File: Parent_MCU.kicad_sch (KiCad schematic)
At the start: 56 parts, among them Y1 Crystal_GND24

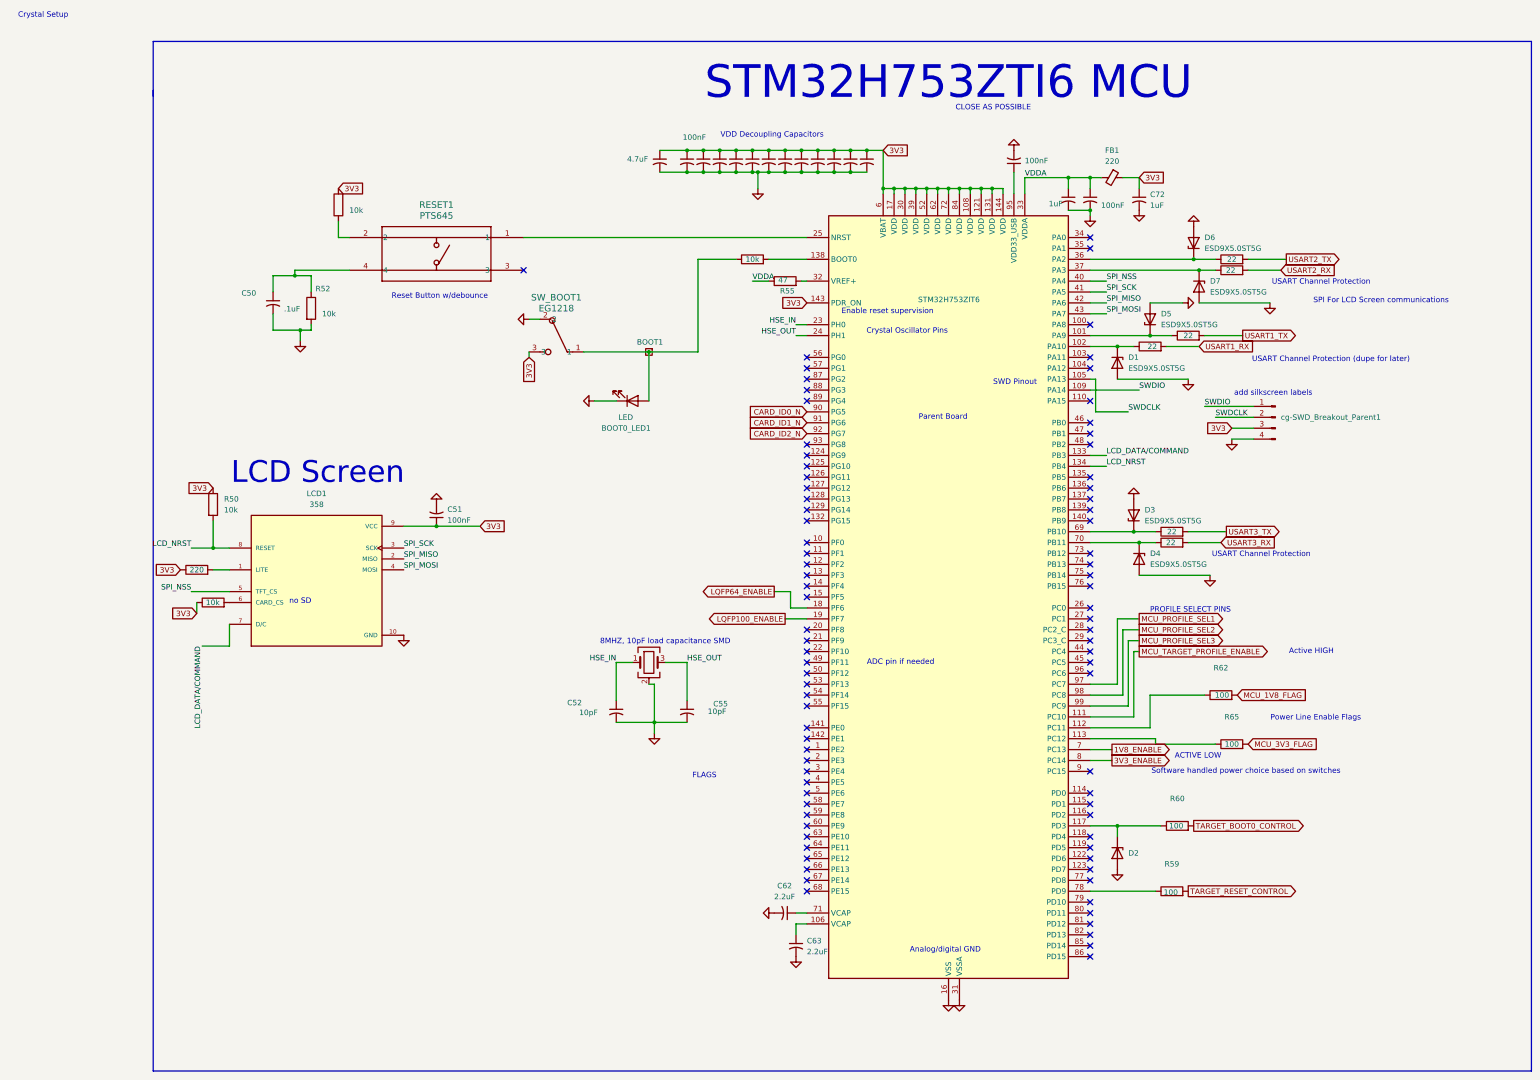
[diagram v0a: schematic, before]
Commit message: finished routing
//TODO
-> add mechanical support
-> daughter board
-> recheck nodes/conections
-> silk screen
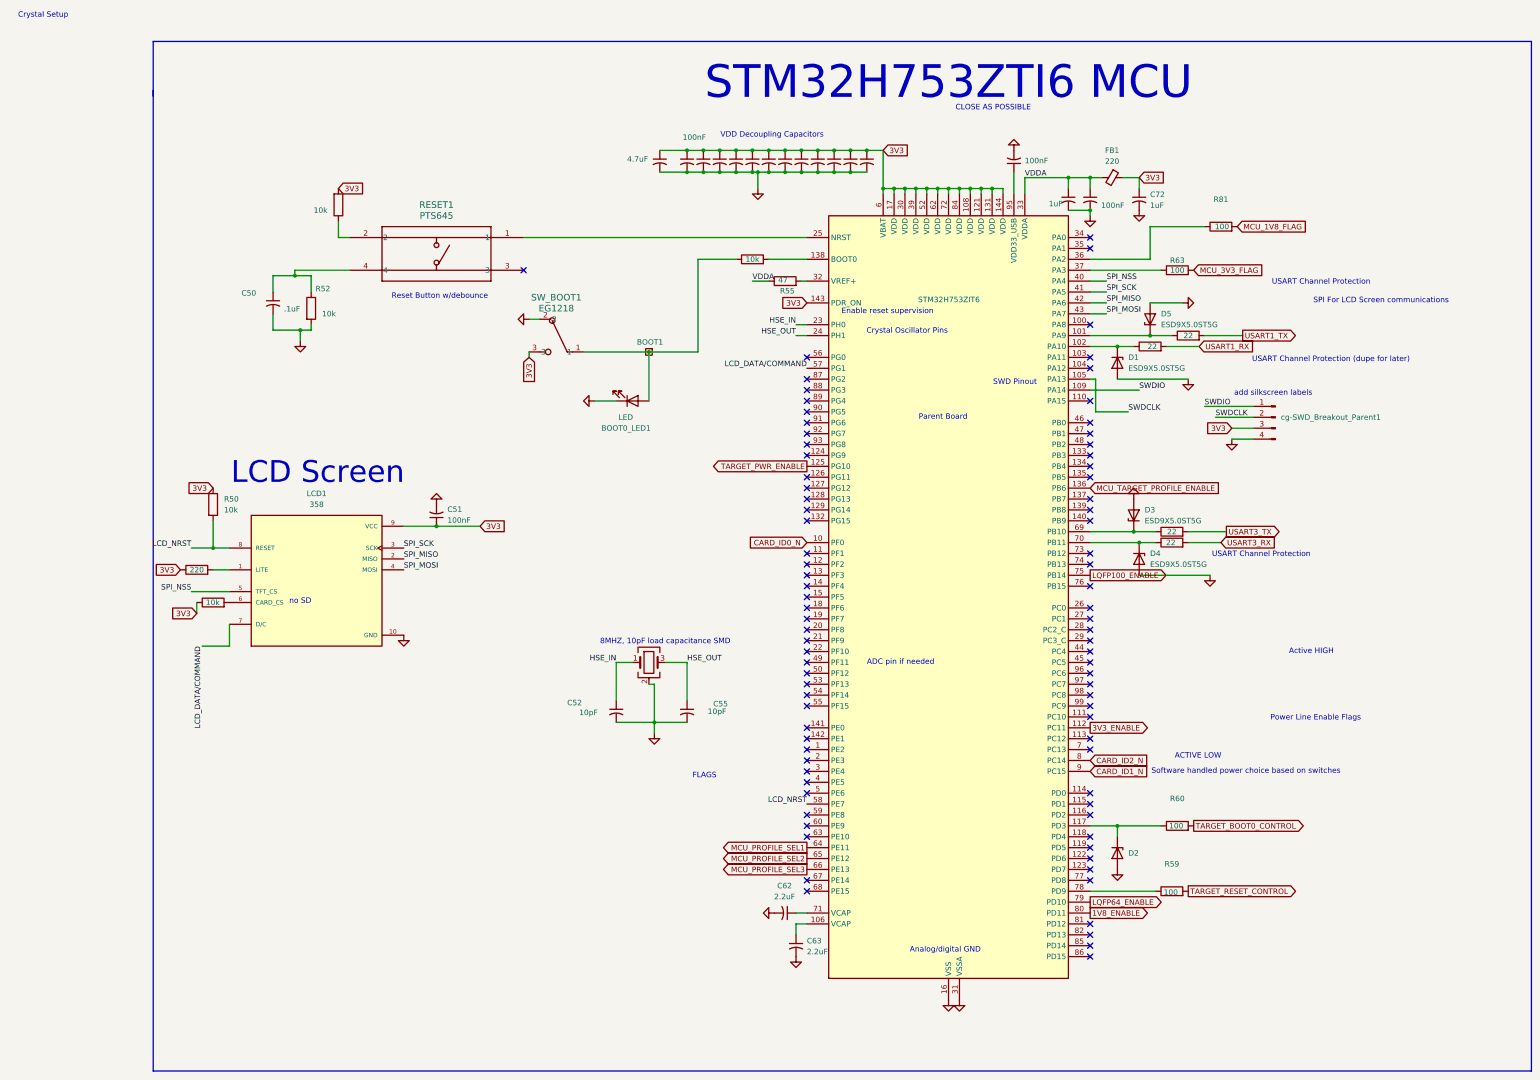
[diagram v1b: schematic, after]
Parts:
- removed D6, D7: ESD9X5.0ST5G, Diode_SMD:D_SOD-923, symbol Diode:PTVS5V0Z1USK
- removed R62, R65: 100, Resistor_SMD:R_0603_1608Metric, symbol Device:R
- removed R64: 22, Resistor_SMD:R_0603_1608Metric, symbol Device:R
- added R81: 100, Resistor_SMD:R_0603_1608Metric, symbol Device:R
- R63: value 22 -> 100
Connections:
- net USART2_TX is gone; now on net MCU_3V3_FLAG: R63.2
- net 1V8_ENABLE: now also STM32H1.80 (PD11); no longer STM32H1.7 (PC13)
- net 3V3_ENABLE: now also STM32H1.112 (PC11); no longer STM32H1.8 (PC14)
- net CARD_ID0_N: now also STM32H1.10 (PF0); no longer STM32H1.90 (PG5)
- net CARD_ID1_N: now also STM32H1.9 (PC15); no longer STM32H1.91 (PG6)
- net CARD_ID2_N: now also STM32H1.8 (PC14); no longer STM32H1.92 (PG7)
- net LCD_DATA/COMMAND: now also STM32H1.57 (PG1); no longer STM32H1.133 (PB3)
- net LCD_NRST: now also STM32H1.58 (PE7); no longer STM32H1.134 (PB4)
- net LQFP100_ENABLE: now also STM32H1.75 (PB14); no longer STM32H1.19 (PF7)
- net LQFP64_ENABLE: now also STM32H1.79 (PD10); no longer STM32H1.18 (PF6)
- net MCU_1V8_FLAG: now also R81.2
- net MCU_PROFILE_SEL1: now also STM32H1.64 (PE11); no longer STM32H1.97 (PC7)
- net MCU_PROFILE_SEL2: now also STM32H1.65 (PE12); no longer STM32H1.98 (PC8)
- net MCU_PROFILE_SEL3: now also STM32H1.66 (PE13); no longer STM32H1.99 (PC9)
- net MCU_TARGET_PROFILE_ENABLE: now also STM32H1.136 (PB6); no longer STM32H1.111 (PC10)
- net at STM32H1.36 (PA2): now also R81.1; no longer R63.1
- net TARGET_PWR_ENABLE: now reaches STM32H1.125 (PG10)
- net at STM32H1.37 (PA3): now also R63.1
- no-connect marks 84 -> 85
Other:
- note removed: "PROFILE SELECT PINS"

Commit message: sockets
fdsfd
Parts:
- renumbered R63 to R60, R60 to R61, R61 to R62, R81 to R63
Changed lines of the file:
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@@
 		(in_pos_files yes)
 		(dnp no)
-		(property "Reference" "R60"
+		(property "Reference" "R61"
 			(at 273.05 200.66 90)
 			(show_name no)
@@
 			(project "CG Files"
 				(path "/bab4cc86-0c89-4bf5-848e-e99340a6180d/d2a8d785-8eb6-410a-b71c-0410f8135e6c"
-					(reference "R60")
+					(reference "R61")
 					(unit 1)
 				)
@@
 		(in_pos_files yes)
 		(dnp no)
-		(property "Reference" "R63"
+		(property "Reference" "R60"
 			(at 273.05 75.184 90)
 			(show_name no)
@@
 			(project "CG Files"
 				(path "/bab4cc86-0c89-4bf5-848e-e99340a6180d/d2a8d785-8eb6-410a-b71c-0410f8135e6c"
-					(reference "R63")
+					(reference "R60")
 					(unit 1)
 				)
@@
 		(in_pos_files yes)
 		(dnp no)
-		(property "Reference" "R61"
+		(property "Reference" "R62"
 			(at 275.59 86.36 90)
 			(hide yes)
@@
 			(project "CG Files"
 				(path "/bab4cc86-0c89-4bf5-848e-e99340a6180d/d2a8d785-8eb6-410a-b71c-0410f8135e6c"
-					(reference "R61")
+					(reference "R62")
 					(unit 1)
 				)
@@
 		(in_pos_files yes)
 		(dnp no)
-		(property "Reference" "R81"
+		(property "Reference" "R63"
 			(at 283.21 60.96 90)
 			(show_name no)
@@
 			(project "CG Files"
 				(path "/bab4cc86-0c89-4bf5-848e-e99340a6180d/d2a8d785-8eb6-410a-b71c-0410f8135e6c"
-					(reference "R81")
+					(reference "R63")
 					(unit 1)
 				)

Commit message: Update
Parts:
- BOOT0_LED1, C50, C51, C52, C53, C54, C55, C56, C57, C58, C59, C60, C61, C62, C63, C64, C65, C66, C67, C68, C69, C70, C71, C72, FB1, R49, R50, R51, R52, R53, R54, R55, R56, R57, R58, R59, R60, R61, R62, R63: KiLib_Generator (none) -> SMD_2terminal_chip_molded
- LCD1, cg-SWD_Breakout_Parent1: KiLib_Generator (none) -> connector/pin_header_socket
- STM32H1: KiLib_Generator (none) -> package/gullwing
- Y1: KiLib_Generator (none) -> crystal_resonator_oscillator; private KLC_S4.1 -> (none)
